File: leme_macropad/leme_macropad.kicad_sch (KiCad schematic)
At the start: 41 parts, among them J1 USB_C_Receptacle_USB2.0_16P, U2 NCP1117-3.3_SOT223, U5 USBLC6-2SC6

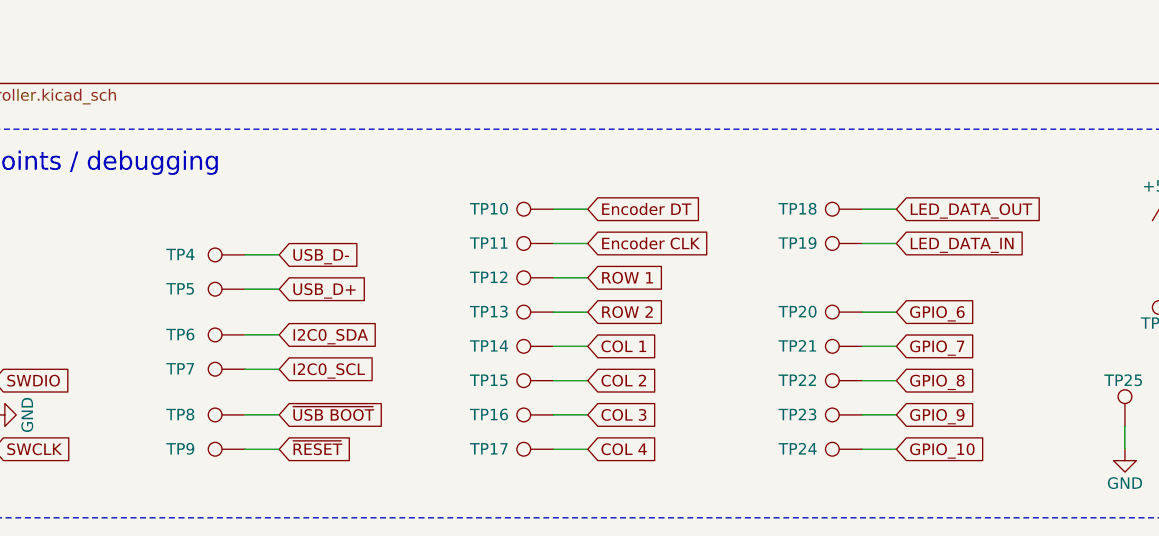
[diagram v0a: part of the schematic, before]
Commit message: Removes unused tespoints
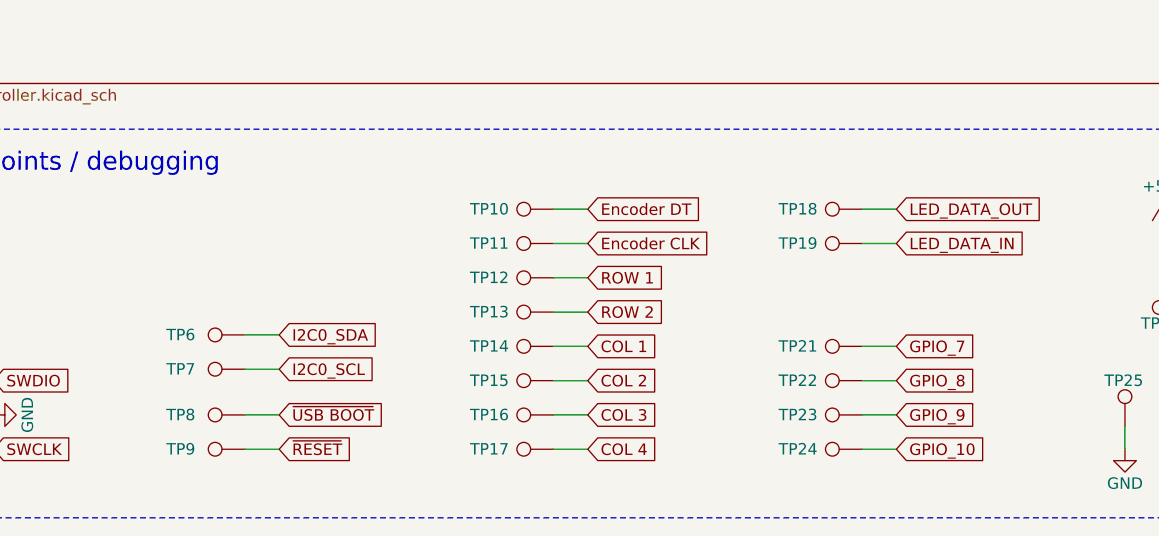
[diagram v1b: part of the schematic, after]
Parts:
- removed TP20, TP4, TP5: TestPoint, TestPoint:TestPoint_Pad_D1.0mm, symbol Connector:TestPoint

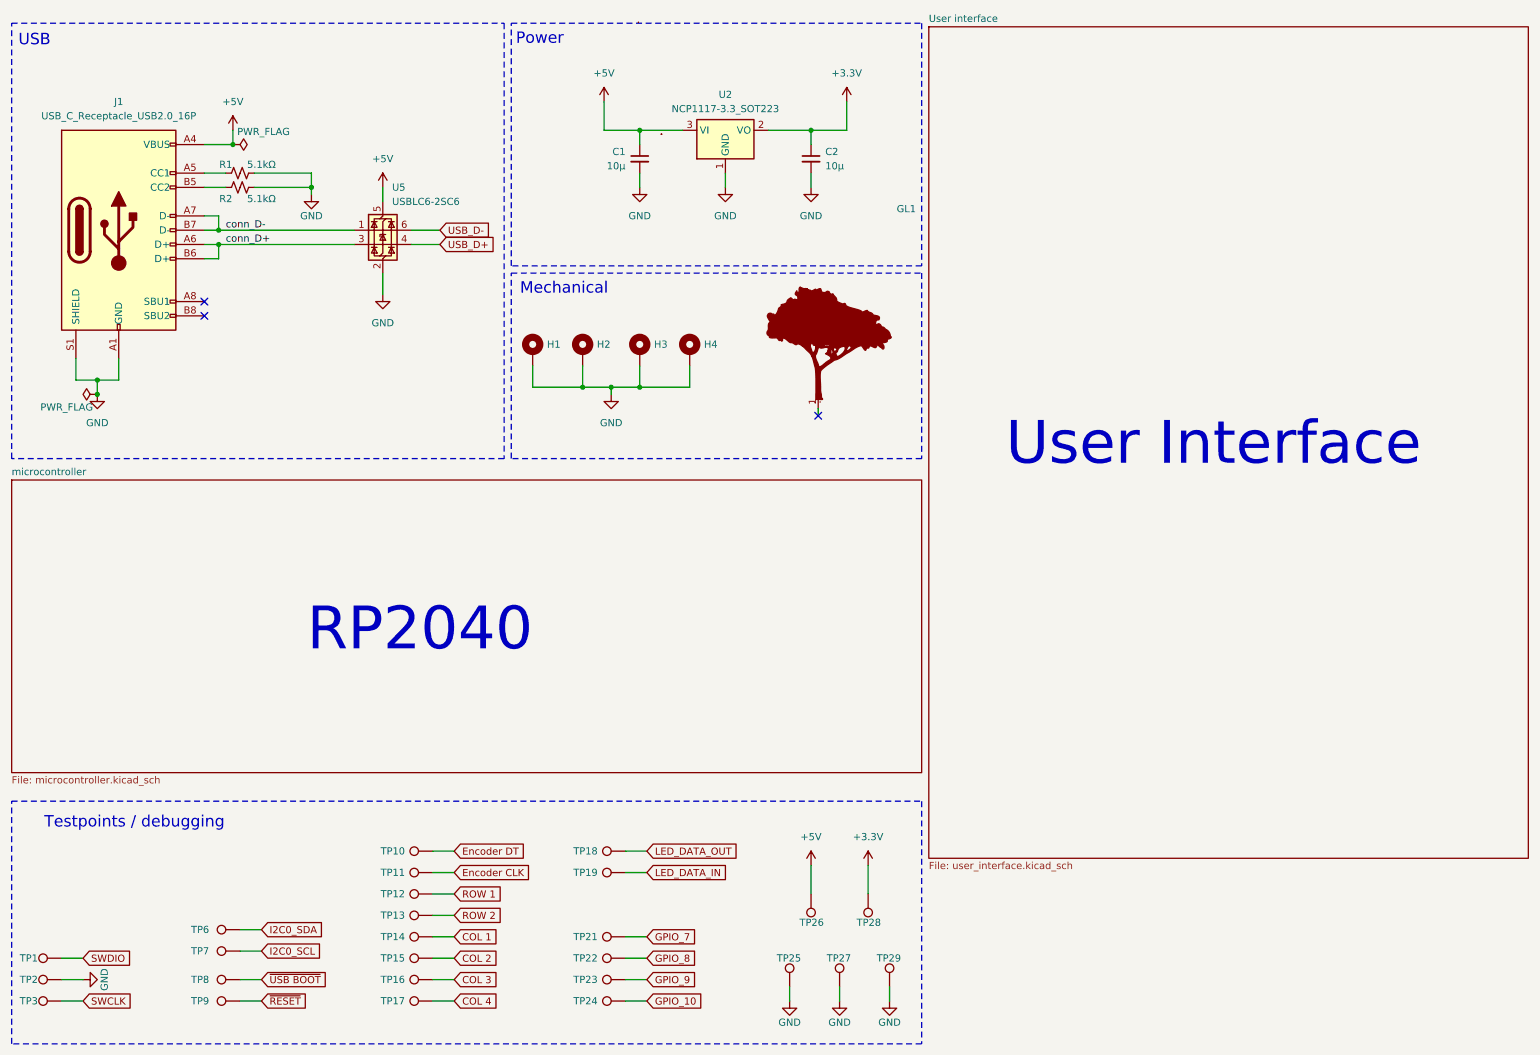
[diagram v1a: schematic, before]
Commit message: Reassigns designators based on component location on the PCB
Kicad 6 has a tool for that: geographical reannotate.
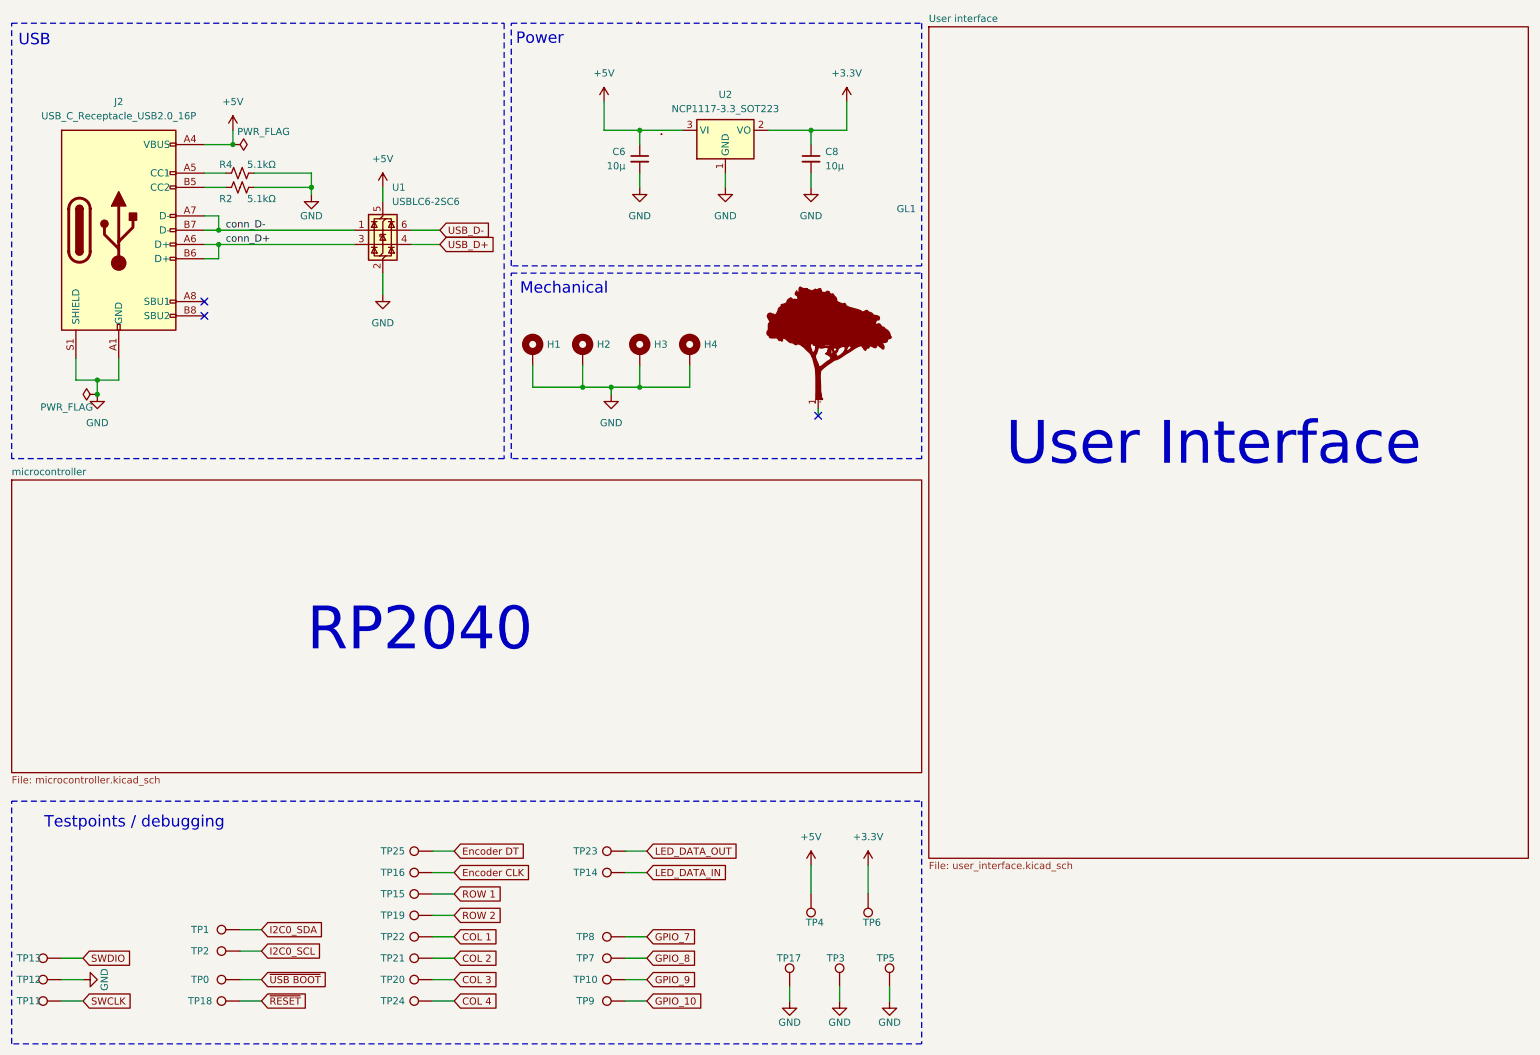
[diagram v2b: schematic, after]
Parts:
- renumbered C1 to C6, C2 to C8, J1 to J2, R1 to R4, TP8 to TP0, TP6 to TP1, TP23 to TP10, TP3 to TP11, TP2 to TP12, TP1 to TP13, TP19 to TP14, TP12 to TP15, TP11 to TP16, TP25 to TP17, TP9 to TP18, TP13 to TP19, TP7 to TP2, TP16 to TP20, TP15 to TP21, TP14 to TP22, TP18 to TP23, TP17 to TP24, TP10 to TP25, TP27 to TP3, TP26 to TP4, TP29 to TP5, TP28 to TP6, TP22 to TP7, TP21 to TP8, TP24 to TP9, U5 to U1
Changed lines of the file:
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@@
 		(on_board yes)
 		(dnp no)
-		(property "Reference" "TP16"
+		(property "Reference" "TP20"
 			(at 81.788 184.15 90)
 			(effects
@@
 			(project "leme_macropad"
 				(path "/a37365a2-c635-4451-9354-78f9e753d687"
-					(reference "TP16")
+					(reference "TP20")
 					(unit 1)
 				)
@@
 		(on_board yes)
 		(dnp no)
-		(property "Reference" "TP11"
+		(property "Reference" "TP16"
 			(at 81.788 165.1 90)
 			(effects
@@
 			(project "leme_macropad"
 				(path "/a37365a2-c635-4451-9354-78f9e753d687"
-					(reference "TP11")
+					(reference "TP16")
 					(unit 1)
 				)
@@
 		(on_board yes)
 		(dnp no)
-		(property "Reference" "TP28"
+		(property "Reference" "TP6"
 			(at 168.656 173.99 0)
 			(effects
@@
 			(project "leme_macropad"
 				(path "/a37365a2-c635-4451-9354-78f9e753d687"
-					(reference "TP28")
+					(reference "TP6")
 					(unit 1)
 				)
@@
 		(on_board yes)
 		(dnp no)
-		(property "Reference" "TP1"
+		(property "Reference" "TP13"
 			(at 17.018 180.34 90)
 			(effects
@@
 			(project "leme_macropad"
 				(path "/a37365a2-c635-4451-9354-78f9e753d687"
-					(reference "TP1")
+					(reference "TP13")
 					(unit 1)
 				)
@@
 		(on_board yes)
 		(dnp no)
-		(property "Reference" "TP9"
+		(property "Reference" "TP18"
 			(at 47.498 187.96 90)
 			(effects
@@
 			(project "leme_macropad"
 				(path "/a37365a2-c635-4451-9354-78f9e753d687"
-					(reference "TP9")
+					(reference "TP18")
 					(unit 1)
 				)
@@
 		(dnp no)
 		(fields_autoplaced yes)
-		(property "Reference" "J1"
+		(property "Reference" "J2"
 			(at 33.02 27.94 0)
 			(effects
@@
 			(project ""
 				(path "/a37365a2-c635-4451-9354-78f9e753d687"
-					(reference "J1")
+					(reference "J2")
 					(unit 1)
 				)
@@
 		(on_board yes)
 		(dnp no)
-		(property "Reference" "TP12"
+		(property "Reference" "TP15"
 			(at 81.788 168.91 90)
 			(effects
@@
 			(project "leme_macropad"
 				(path "/a37365a2-c635-4451-9354-78f9e753d687"
-					(reference "TP12")
+					(reference "TP15")
 					(unit 1)
 				)
@@
 		(on_board yes)
 		(dnp no)
-		(property "Reference" "TP8"
+		(property "Reference" "TP0"
 			(at 47.498 184.15 90)
 			(effects
@@
 			(project "leme_macropad"
 				(path "/a37365a2-c635-4451-9354-78f9e753d687"
-					(reference "TP8")
+					(reference "TP0")
 					(unit 1)
 				)
@@
 		(on_board yes)
 		(dnp no)
-		(property "Reference" "TP7"
+		(property "Reference" "TP2"
 			(at 47.498 179.07 90)
 			(effects
@@
 			(project "leme_macropad"
 				(path "/a37365a2-c635-4451-9354-78f9e753d687"
-					(reference "TP7")
+					(reference "TP2")
 					(unit 1)
 				)
@@
 		(on_board yes)
 		(dnp no)
-		(property "Reference" "TP13"
+		(property "Reference" "TP19"
 			(at 81.788 172.72 90)
 			(effects
@@
 			(project "leme_macropad"
 				(path "/a37365a2-c635-4451-9354-78f9e753d687"
-					(reference "TP13")
+					(reference "TP19")
 					(unit 1)
 				)
@@
 		(on_board yes)
 		(dnp no)
-		(property "Reference" "TP19"
+		(property "Reference" "TP14"
 			(at 116.078 165.1 90)
 			(effects
@@
 			(project "leme_macropad"
 				(path "/a37365a2-c635-4451-9354-78f9e753d687"
-					(reference "TP19")
+					(reference "TP14")
 					(unit 1)
 				)
@@
 		(on_board yes)
 		(dnp no)
-		(property "Reference" "TP29"
+		(property "Reference" "TP5"
 			(at 167.894 180.34 0)
 			(effects
@@
 			(project "leme_macropad"
 				(path "/a37365a2-c635-4451-9354-78f9e753d687"
-					(reference "TP29")
+					(reference "TP5")
 					(unit 1)
 				)
@@
 		(on_board yes)
 		(dnp no)
-		(property "Reference" "TP6"
+		(property "Reference" "TP1"
 			(at 47.498 175.26 90)
 			(effects
@@
 			(project "leme_macropad"
 				(path "/a37365a2-c635-4451-9354-78f9e753d687"
-					(reference "TP6")
+					(reference "TP1")
 					(unit 1)
 				)
@@
 		(on_board yes)
 		(dnp no)
-		(property "Reference" "U5"
+		(property "Reference" "U1"
 			(at 81.6611 43.18 0)
 			(effects
@@
 			(project ""
 				(path "/a37365a2-c635-4451-9354-78f9e753d687"
-					(reference "U5")
+					(reference "U1")
 					(unit 1)
 				)
@@
 		(on_board yes)
 		(dnp no)
-		(property "Reference" "TP15"
+		(property "Reference" "TP21"
 			(at 81.788 180.34 90)
 			(effects
@@
 			(project "leme_macropad"
 				(path "/a37365a2-c635-4451-9354-78f9e753d687"
-					(reference "TP15")
+					(reference "TP21")
 					(unit 1)
 				)
@@
 		(on_board yes)
 		(dnp no)
-		(property "Reference" "C2"
+		(property "Reference" "C8"
 			(at 158.75 36.8362 0)
 			(effects
@@
 			(project "leme_macropad"
 				(path "/a37365a2-c635-4451-9354-78f9e753d687"
-					(reference "C2")
+					(reference "C8")
 					(unit 1)
 				)
@@
 		(on_board yes)
 		(dnp no)
-		(property "Reference" "TP17"
+		(property "Reference" "TP24"
 			(at 81.788 187.96 90)
 			(effects
@@
 			(project "leme_macropad"
 				(path "/a37365a2-c635-4451-9354-78f9e753d687"
-					(reference "TP17")
+					(reference "TP24")
 					(unit 1)
 				)
@@
 		(on_board yes)
 		(dnp no)
-		(property "Reference" "TP24"
+		(property "Reference" "TP9"
 			(at 116.078 187.96 90)
 			(effects
@@
 			(project "leme_macropad"
 				(path "/a37365a2-c635-4451-9354-78f9e753d687"
-					(reference "TP24")
+					(reference "TP9")
 					(unit 1)
 				)
@@
 		(on_board yes)
 		(dnp no)
-		(property "Reference" "TP18"
+		(property "Reference" "TP23"
 			(at 116.078 161.29 90)
 			(effects
@@
 			(project "leme_macropad"
 				(path "/a37365a2-c635-4451-9354-78f9e753d687"
-					(reference "TP18")
+					(reference "TP23")
 					(unit 1)
 				)
@@
 		(on_board yes)
 		(dnp no)
-		(property "Reference" "TP23"
+		(property "Reference" "TP10"
 			(at 116.078 184.15 90)
 			(effects
@@
 			(project "leme_macropad"
 				(path "/a37365a2-c635-4451-9354-78f9e753d687"
-					(reference "TP23")
+					(reference "TP10")
 					(unit 1)
 				)
@@
 		(on_board yes)
 		(dnp no)
-		(property "Reference" "TP25"
+		(property "Reference" "TP17"
 			(at 150.114 180.34 0)
 			(effects
@@
 			(project ""
 				(path "/a37365a2-c635-4451-9354-78f9e753d687"
-					(reference "TP25")
+					(reference "TP17")
 					(unit 1)
 				)
@@
 		(on_board yes)
 		(dnp no)
-		(property "Reference" "TP26"
+		(property "Reference" "TP4"
 			(at 158.496 173.99 0)
 			(effects
@@
 			(project "leme_macropad"
 				(path "/a37365a2-c635-4451-9354-78f9e753d687"
-					(reference "TP26")
+					(reference "TP4")
 					(unit 1)
 				)
@@
 		(on_board yes)
 		(dnp no)
-		(property "Reference" "TP3"
+		(property "Reference" "TP11"
 			(at 17.018 187.96 90)
 			(effects
@@
 			(project ""
 				(path "/a37365a2-c635-4451-9354-78f9e753d687"
-					(reference "TP3")
+					(reference "TP11")
 					(unit 1)
 				)
@@
 		(on_board yes)
 		(dnp no)
-		(property "Reference" "TP2"
+		(property "Reference" "TP12"
 			(at 17.018 184.15 90)
 			(effects
@@
 			(project "leme_macropad"
 				(path "/a37365a2-c635-4451-9354-78f9e753d687"
-					(reference "TP2")
+					(reference "TP12")
 					(unit 1)
 				)
@@
 		(on_board yes)
 		(dnp no)
-		(property "Reference" "TP21"
+		(property "Reference" "TP8"
 			(at 116.078 176.53 90)
 			(effects
@@
 			(project "leme_macropad"
 				(path "/a37365a2-c635-4451-9354-78f9e753d687"
-					(reference "TP21")
+					(reference "TP8")
 					(unit 1)
 				)
@@
 		(on_board yes)
 		(dnp no)
-		(property "Reference" "C1"
+		(property "Reference" "C6"
 			(at 123.19 36.8362 0)
 			(effects
@@
 			(project ""
 				(path "/a37365a2-c635-4451-9354-78f9e753d687"
-					(reference "C1")
+					(reference "C6")
 					(unit 1)
 				)
@@
 		(on_board yes)
 		(dnp no)
-		(property "Reference" "TP14"
+		(property "Reference" "TP22"
 			(at 81.788 176.53 90)
 			(effects
@@
 			(project "leme_macropad"
 				(path "/a37365a2-c635-4451-9354-78f9e753d687"
-					(reference "TP14")
+					(reference "TP22")
 					(unit 1)
 				)
@@
 		(on_board yes)
 		(dnp no)
-		(property "Reference" "TP22"
+		(property "Reference" "TP7"
 			(at 116.078 180.34 90)
 			(effects
@@
 			(project "leme_macropad"
 				(path "/a37365a2-c635-4451-9354-78f9e753d687"
-					(reference "TP22")
+					(reference "TP7")
 					(unit 1)
 				)
@@
 		(on_board yes)
 		(dnp no)
-		(property "Reference" "R1"
+		(property "Reference" "R4"
 			(at 52.07 39.116 90)
 			(effects
@@
 			(project "leme_macropad"
 				(path "/a37365a2-c635-4451-9354-78f9e753d687"
-					(reference "R1")
+					(reference "R4")
 					(unit 1)
 				)
@@
 		(on_board yes)
 		(dnp no)
-		(property "Reference" "TP27"
+		(property "Reference" "TP3"
 			(at 159.004 180.34 0)
 			(effects
@@
 			(project "leme_macropad"
 				(path "/a37365a2-c635-4451-9354-78f9e753d687"
-					(reference "TP27")
+					(reference "TP3")
 					(unit 1)
 				)
@@
 		(on_board yes)
 		(dnp no)
-		(property "Reference" "TP10"
+		(property "Reference" "TP25"
 			(at 81.788 161.29 90)
 			(effects
@@
 			(project "leme_macropad"
 				(path "/a37365a2-c635-4451-9354-78f9e753d687"
-					(reference "TP10")
+					(reference "TP25")
 					(unit 1)
 				)
